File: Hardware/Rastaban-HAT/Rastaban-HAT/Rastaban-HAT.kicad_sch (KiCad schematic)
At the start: 62 parts, among them J1 1778780, J10 GPIO, J11 Conn_01x06_Male, J2 1778780, J3 1778780, J4 Screw_Terminal_01x02, J5 Jack-DC 12V+, J6 SM04B-SRSS-TB(LF)(SN), J7 Screw_Terminal_01x02, J8 Screw_Terminal_01x02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

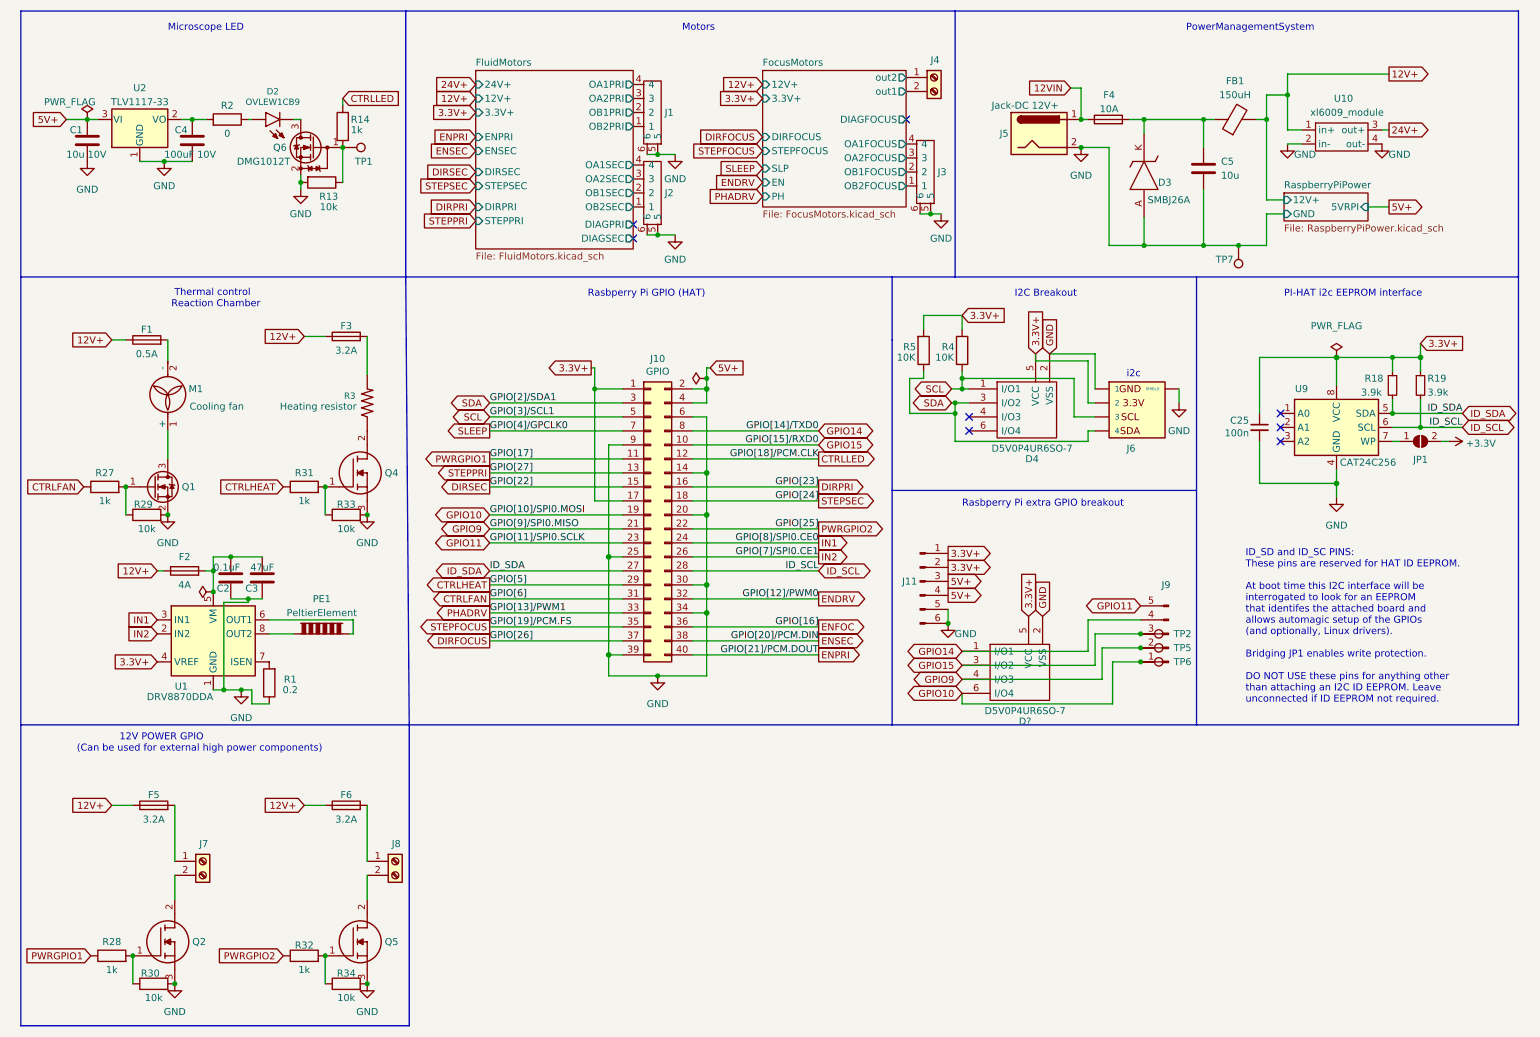
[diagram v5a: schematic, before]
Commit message: Schematic v1.2
added johan brussen's advice
written software for stepper motor drivers
test report written.
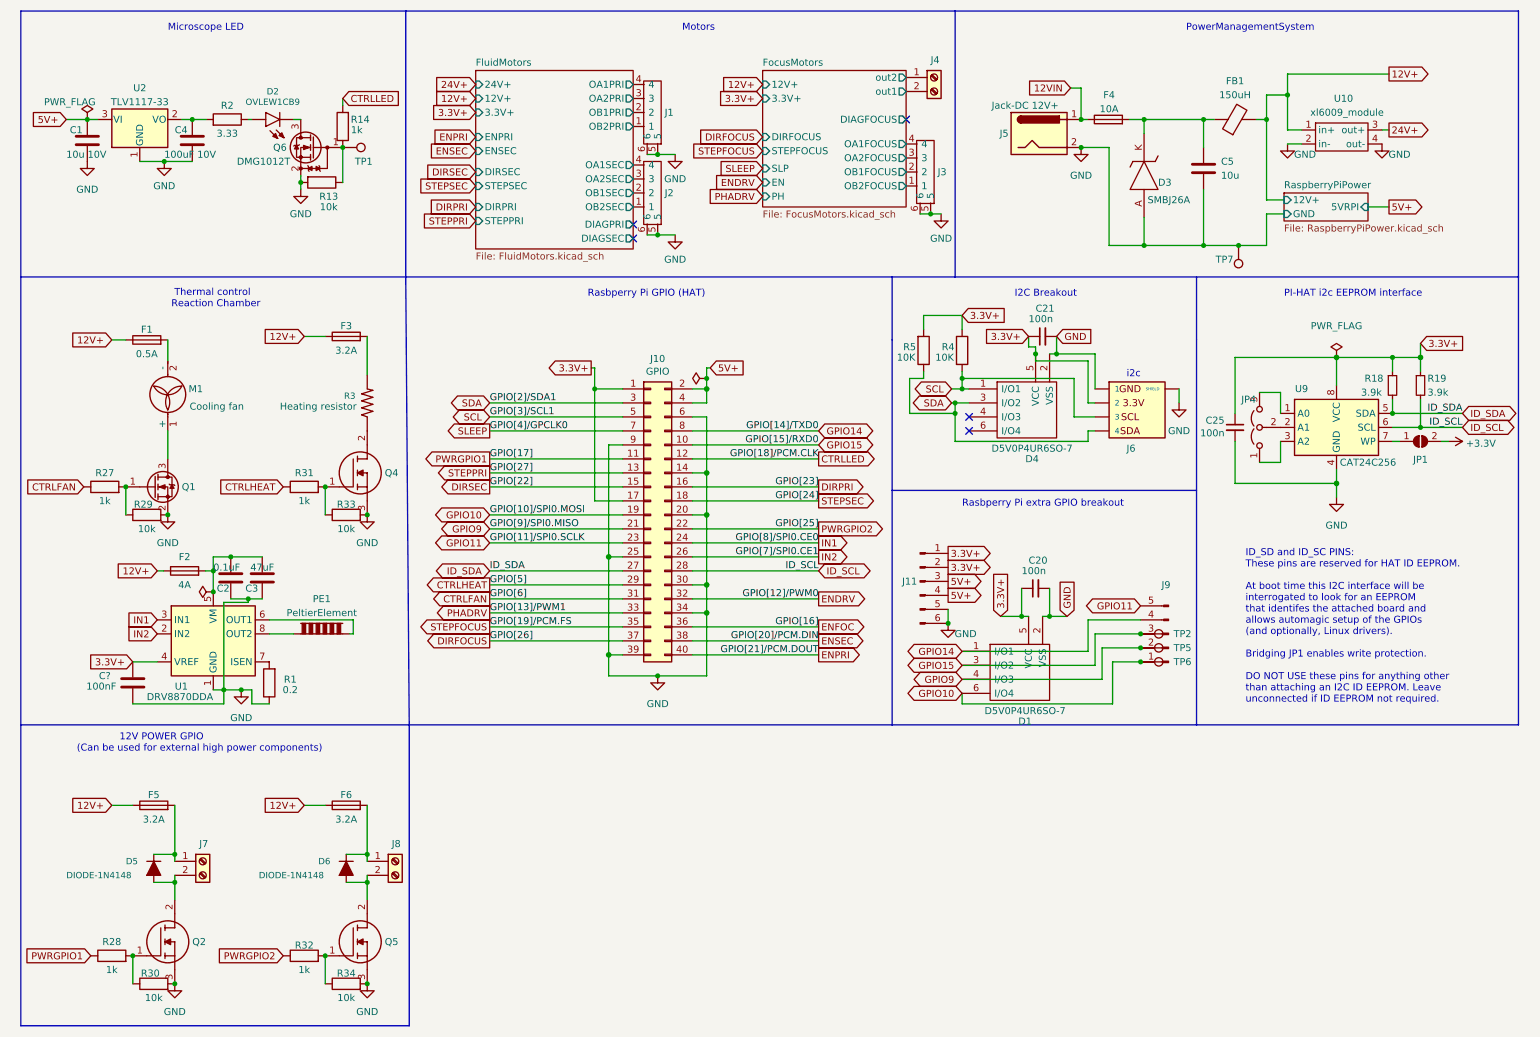
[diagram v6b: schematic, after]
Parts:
- added C20, C21: 100n, Capacitor_SMD:C_1206_3216Metric_Pad1.33x1.80mm_HandSolder, symbol Device:C_Small
- added C?: 100nF, Capacitor_SMD:C_1206_3216Metric_Pad1.33x1.80mm_HandSolder, symbol Device:C
- added D5, D6: DIODE-1N4148, DIODE-1N4148, symbol SparkFun-DiscreteSemi:DIODE-1N4148
- added JP4: Jumper_3_Open, symbol Jumper:Jumper_3_Open
- R2: value 0 -> 3.33; Purpose (none) -> current limit for led
- gave numbers to parts that had none: 1
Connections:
- net 3.3V+: now also C20.1, C21.1, C?.2
- net GND: now also C20.2, C21.2, C?.1
- net at F5.2, J7.1 (Pin_1): now also D5.C
- net at J7.2 (Pin_2), Q2.2: now also D5.A
- net at F6.2, J8.1 (Pin_1): now also D6.C
- net at J8.2 (Pin_2), Q5.2: now also D6.A
- net at U9.1 (A0): now also JP4.3 (B)
- net at U9.2 (A1): now also JP4.2 (C)
- net at U9.3 (A2): now also JP4.1 (A)
- no-connect marks 8 -> 5
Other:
- moved on the sheet: C25

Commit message: added new libarries and jlcpcb part plugin
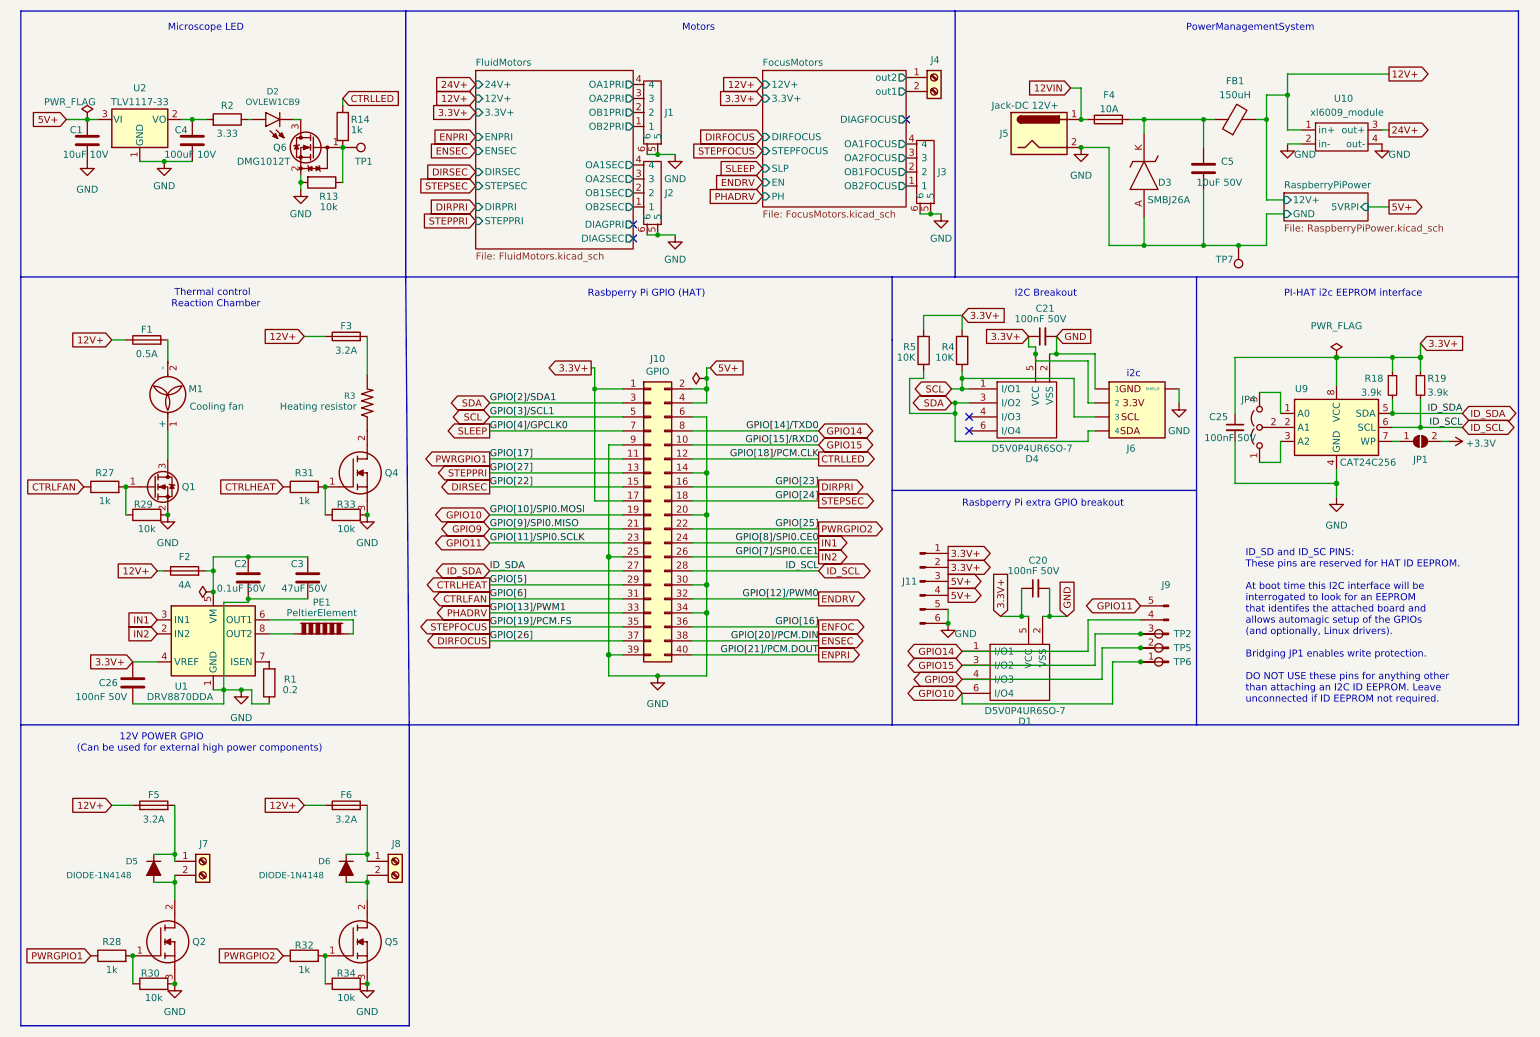
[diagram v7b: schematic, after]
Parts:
- C1: value 10u 10V -> 10uF 10V; footprint (none) -> Capacitor_SMD:C_0805_2012Metric_Pad1.18x1.45mm_HandSolder; LCSC (none) -> C513765; Manufacturer_Part_Number (none) -> C513765
- C2: value 0.1uF -> 0.1uF 50V; footprint Capacitor_SMD:C_1206_3216Metric_Pad1.33x1.80mm_HandSolder -> Capacitor_SMD:C_0805_2012Metric_Pad1.18x1.45mm_HandSolder; LCSC (none) -> C28061
- C20, C21, C25: value 100n -> 100nF 50V; footprint Capacitor_SMD:C_1206_3216Metric_Pad1.33x1.80mm_HandSolder -> Capacitor_SMD:C_0805_2012Metric_Pad1.18x1.45mm_HandSolder; LCSC (none) -> C49678
- C26: renamed from C?; value 100nF -> 100nF 50V; footprint Capacitor_SMD:C_1206_3216Metric_Pad1.33x1.80mm_HandSolder -> Capacitor_SMD:C_0805_2012Metric_Pad1.18x1.45mm_HandSolder; LCSC (none) -> C49678
- C3: value 47uF -> 47uF 50V; footprint Capacitor_SMD:C_1206_3216Metric_Pad1.33x1.80mm_HandSolder -> Capacitor_SMD:C_0805_2012Metric_Pad1.18x1.45mm_HandSolder; LCSC (none) -> C2918513; Manufacturer_Part_Number (none) -> C2918513
- C4: footprint Capacitor_SMD:C_1206_3216Metric_Pad1.33x1.80mm_HandSolder -> Capacitor_SMD:C_0805_2012Metric_Pad1.18x1.45mm_HandSolder; LCSC (none) -> C3339; Manufacturer_Part_Number (none) -> C3339
- C5: value 10u -> 10uF 50V; footprint Capacitor_SMD:C_1206_3216Metric_Pad1.33x1.80mm_HandSolder -> Capacitor_SMD:C_0805_2012Metric_Pad1.18x1.45mm_HandSolder; LCSC (none) -> C440198
- D1, D4: footprint (none) -> SamacSys_Parts:SOT95P285X140-6N; LCSC (none) -> C531179
- D2: footprint SmacSYs:OVLEW1CB9 -> SamacSys_Parts:OVLEW1CB9
- D3: footprint Snapeda:DIOM4336X265N -> SamacSys_Parts:DIOM5436X261N; LCSC (none) -> C10216
- D5, D6: footprint DIODE-1N4148 -> Diode_SMD:D_1206_3216Metric_Pad1.42x1.75mm_HandSolder; LCSC (none) -> C2128
- J1, J2, J3: footprint SmacSYs:1778780 -> SamacSys_Parts:1778780; LCSC (none) -> C5173835
- J6: footprint Snapeda:JST_SM04B-SRSS-TB(LF)(SN) -> SamacSys_Parts:SM04BHCHKTBLFSN; LCSC (none) -> C160404; Manufacturer_Part_Number (none) -> C160404
- J9: footprint (none) -> Connector_PinHeader_2.54mm:PinHeader_1x05_P2.54mm_Vertical
- JP4: footprint (none) -> Jumper:SolderJumper-3_P1.3mm_Open_Pad1.0x1.5mm_NumberLabels
- Q2, Q4, Q5: footprint SmacSYs:IRL540SPBF -> SamacSys_Parts:IRL540SPBF
- R1, R13, R14, R18, R19, R27, R28, R29, R30, R31, R32, R33, R34, R4, R5: footprint Resistor_SMD:R_1206_3216Metric_Pad1.30x1.75mm_HandSolder -> Resistor_SMD:R_0805_2012Metric_Pad1.20x1.40mm_HandSolder
- R2: footprint (none) -> Resistor_SMD:R_0805_2012Metric_Pad1.20x1.40mm_HandSolder
- U2: footprint (none) -> SamacSys_Parts:SOT230P700X180-4N
- U9: footprint Footprints:SOIC127P600X175-8N -> SamacSys_Parts:SOIC127P600X175-8N
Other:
- moved on the sheet: C2, C3

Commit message: updated footprints
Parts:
- J6: footprint SamacSys_Parts:SM04BHCHKTBLFSN -> SnapEDA Library:JST_SM04B-SRSS-TB(LF)(SN)
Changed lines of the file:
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@@
       (effects (font (size 1.27 1.27)) (justify left) hide)
     )
-    (property "Footprint" "SamacSys_Parts:SM04BHCHKTBLFSN" (id 2) (at 203.835 93.98 0)
+    (property "Footprint" "SnapEDA Library:JST_SM04B-SRSS-TB(LF)(SN)" (id 2) (at 203.835 93.98 0)
       (effects (font (size 1.27 1.27)) (justify left bottom) hide)
     )
@@
     )
     (path "/a59c5d3d-4ea0-4b08-99c1-38f965204418"
-      (reference "J6") (unit 1) (value "SM04B-SRSS-TB(LF)(SN)") (footprint "SamacSys_Parts:SM04BHCHKTBLFSN")
+      (reference "J6") (unit 1) (value "SM04B-SRSS-TB(LF)(SN)") (footprint "SnapEDA Library:JST_SM04B-SRSS-TB(LF)(SN)")
     )
     (path "/00360c14-430e-4399-9d74-f52e2b63950e"
@@
     )
     (path "/509754cd-dbf1-46e6-965c-38d41c0b6924/c1dc1b77-ffa7-4f69-878e-c9530094aabf"
-      (reference "U3") (unit 1) (value "TMC2208_Carrier") (footprint "")
+      (reference "U3") (unit 1) (value "TMC2208_Carrier") (footprint "SnapEDA Library:MODULE_TMC2208_SILENTSTEPSTICK")
     )
     (path "/509754cd-dbf1-46e6-965c-38d41c0b6924/07c85e68-0bf7-427d-95a2-4df276793fef"
-      (reference "U4") (unit 1) (value "TMC2208_Carrier") (footprint "")
+      (reference "U4") (unit 1) (value "TMC2208_Carrier") (footprint "SnapEDA Library:MODULE_TMC2208_SILENTSTEPSTICK")
     )
     (path "/6c4087b1-d585-4615-84b3-d395a8b5856d/ac0fbcf0-97bf-4099-a5f5-25c63eb93075"
-      (reference "U5") (unit 1) (value "RT7272AGSP") (footprint "")
+      (reference "U5") (unit 1) (value "RT7272AGSP") (footprint "SnapEDA Library:SOIC127P599X175-9N")
     )
     (path "/7b03732c-6b0a-482e-b8e3-ced6ad7436b5/172503d1-ddd9-46cd-8151-cd5fd3ec266e"
-      (reference "U6") (unit 1) (value "TMC2208_Carrier") (footprint "")
+      (reference "U6") (unit 1) (value "TMC2208_Carrier") (footprint "SnapEDA Library:MODULE_TMC2208_SILENTSTEPSTICK")
     )
     (path "/7b03732c-6b0a-482e-b8e3-ced6ad7436b5/1d3758c9-7eb3-42ba-8ec8-545ede1e6fd7"
